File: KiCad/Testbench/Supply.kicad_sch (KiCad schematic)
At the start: 3 parts, among them J21 Conn_02x02_Top_Bottom

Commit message: PCB before first processing
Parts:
- renumbered J21 to J29
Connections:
- net GND is gone; now on net GND-LV_Unfiltered: J29.4 (Pin_4)
- net +24V: now also J29.3 (Pin_3)
- no-connect marks 1 -> 0
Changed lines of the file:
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@@
 	(paper "A4")
+	(junction
+		(at 40.64 44.45)
+		(diameter 0)
+		(color 0 0 0 0)
+	)
 	(junction
 		(at 41.91 66.04)
@@
 	)
 	(junction
+		(at 40.64 46.99)
+		(diameter 0)
+		(color 0 0 0 0)
+	)
+	(junction
 		(at 34.29 55.88)
 		(diameter 0)
 		(color 0 0 0 0)
 	)
-	(no_connect
-		(at 57.15 44.45)
-	)
-	(wire
-		(pts
-			(xy 34.29 46.99) (xy 44.45 46.99)
+	(wire
+		(pts
+			(xy 34.29 46.99) (xy 40.64 46.99)
 		)
 		(stroke
@@
 	(wire
 		(pts
+			(xy 40.64 46.99) (xy 40.64 49.53)
+		)
+		(stroke
+			(width 0)
+			(type default)
+		)
+	)
+	(wire
+		(pts
 			(xy 49.53 59.69) (xy 49.53 66.04)
 		)
@@
 	(wire
 		(pts
-			(xy 74.93 46.99) (xy 74.93 69.85)
+			(xy 62.23 49.53) (xy 62.23 46.99)
 		)
 		(stroke
@@
 	(wire
 		(pts
+			(xy 40.64 46.99) (xy 44.45 46.99)
+		)
+		(stroke
+			(width 0)
+			(type default)
+		)
+	)
+	(wire
+		(pts
 			(xy 34.29 31.75) (xy 34.29 34.29)
 		)
@@
 	(wire
 		(pts
+			(xy 62.23 46.99) (xy 57.15 46.99)
+		)
+		(stroke
+			(width 0)
+			(type default)
+		)
+	)
+	(wire
+		(pts
 			(xy 57.15 66.04) (xy 49.53 66.04)
 		)
@@
 	(wire
 		(pts
+			(xy 40.64 44.45) (xy 40.64 35.56)
+		)
+		(stroke
+			(width 0)
+			(type default)
+		)
+	)
+	(wire
+		(pts
+			(xy 40.64 35.56) (xy 66.04 35.56)
+		)
+		(stroke
+			(width 0)
+			(type default)
+		)
+	)
+	(wire
+		(pts
 			(xy 34.29 46.99) (xy 34.29 55.88)
 		)
@@
 	(wire
 		(pts
+			(xy 40.64 49.53) (xy 62.23 49.53)
+		)
+		(stroke
+			(width 0)
+			(type default)
+		)
+	)
+	(wire
+		(pts
 			(xy 34.29 34.29) (xy 40.64 34.29)
 		)
@@
 	(wire
 		(pts
-			(xy 44.45 44.45) (xy 34.29 44.45)
-		)
-		(stroke
-			(width 0)
-			(type default)
-		)
-	)
-	(wire
-		(pts
-			(xy 57.15 46.99) (xy 74.93 46.99)
+			(xy 40.64 44.45) (xy 34.29 44.45)
+		)
+		(stroke
+			(width 0)
+			(type default)
+		)
+	)
+	(wire
+		(pts
+			(xy 66.04 35.56) (xy 66.04 44.45)
+		)
+		(stroke
+			(width 0)
+			(type default)
+		)
+	)
+	(wire
+		(pts
+			(xy 44.45 44.45) (xy 40.64 44.45)
 		)
 		(stroke
@@
 		(pts
 			(xy 34.29 55.88) (xy 34.29 66.04)
+		)
+		(stroke
+			(width 0)
+			(type default)
+		)
+	)
+	(wire
+		(pts
+			(xy 66.04 44.45) (xy 57.15 44.45)
 		)
 		(stroke
@@
 		)
 	)
-	(label "3-G4"
-		(at 67.31 46.99 0)
-		(fields_autoplaced yes)
-		(effects
-			(font
-				(size 1.27 1.27)
-			)
-			(justify left bottom)
-		)
-	)
 	(label "1-F2"
 		(at 49.53 59.69 0)
@@
 			)
 			(justify left bottom)
-		)
-	)
-	(symbol
-		(lib_id "power:GND")
-		(at 74.93 69.85 0)
-		(unit 1)
-		(exclude_from_sim no)
-		(in_bom yes)
-		(on_board yes)
-		(dnp no)
-		(fields_autoplaced yes)
-		(property "Reference" "#PWR026"
-			(at 74.93 76.2 0)
-			(effects
-				(font
-					(size 1.27 1.27)
-				)
-				(hide yes)
-			)
-		)
-		(property "Value" "GND"
-			(at 74.93 74.93 0)
-			(effects
-				(font
-					(size 1.27 1.27)
-				)
-			)
-		)
-		(property "Footprint" ""
-			(at 74.93 69.85 0)
-			(effects
-				(font
-					(size 1.27 1.27)
-				)
-				(hide yes)
-			)
-		)
-		(property "Datasheet" ""
-			(at 74.93 69.85 0)
-			(effects
-				(font
-					(size 1.27 1.27)
-				)
-				(hide yes)
-			)
-		)
-		(property "Description" "Power symbol creates a global label with name \"GND\" , ground"
-			(at 74.93 69.85 0)
-			(effects
-				(font
-					(size 1.27 1.27)
-				)
-				(hide yes)
-			)
-		)
-		(pin "1"
-		)
-		(instances
-			(project ""
-				(path "/7bff671f-2f7d-4dcb-82cb-7f168fb2ab46/c2512be0-55aa-4b8a-8574-f17326802af0"
-					(reference "#PWR026")
-					(unit 1)
-				)
-			)
 		)
 	)
@@
 		(on_board yes)
 		(dnp no)
-		(property "Reference" "#PWR025"
+		(property "Reference" "#PWR028"
 			(at 49.53 77.47 0)
 			(effects
@@
 			(project "Testbench"
 				(path "/7bff671f-2f7d-4dcb-82cb-7f168fb2ab46/c2512be0-55aa-4b8a-8574-f17326802af0"
-					(reference "#PWR025")
+					(reference "#PWR028")
 					(unit 1)
 				)
@@
 		(dnp no)
 		(fields_autoplaced yes)
-		(property "Reference" "J21"
+		(property "Reference" "J29"
 			(at 50.8 38.1 0)
 			(effects
@@
 			(project ""
 				(path "/7bff671f-2f7d-4dcb-82cb-7f168fb2ab46/c2512be0-55aa-4b8a-8574-f17326802af0"
-					(reference "J21")
+					(reference "J29")
 					(unit 1)
 				)
@@
 		(dnp no)
 		(fields_autoplaced yes)
-		(property "Reference" "#PWR024"
+		(property "Reference" "#PWR027"
 			(at 34.29 35.56 0)
 			(effects
@@
 			(project ""
 				(path "/7bff671f-2f7d-4dcb-82cb-7f168fb2ab46/c2512be0-55aa-4b8a-8574-f17326802af0"
-					(reference "#PWR024")
+					(reference "#PWR027")
 					(unit 1)
 				)

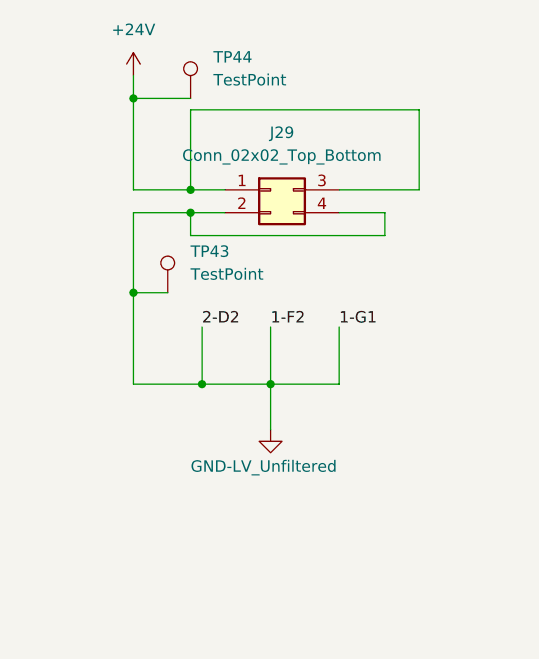
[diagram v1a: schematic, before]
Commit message: Updated for PCBV2 Updated size and added LED.
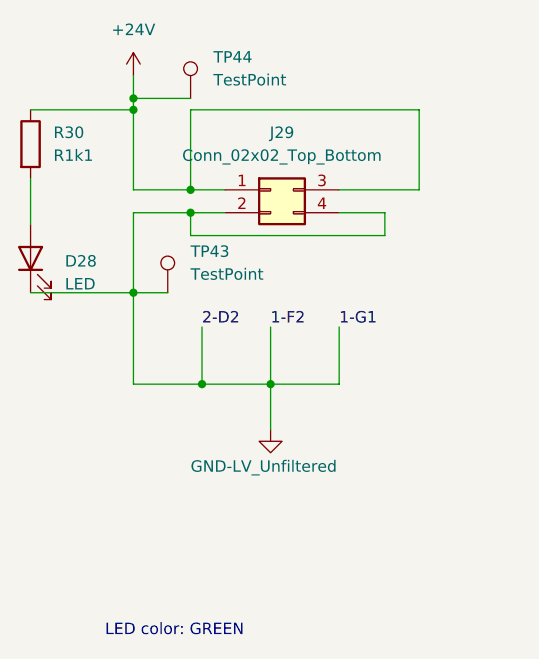
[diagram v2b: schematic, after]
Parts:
- added D28: LED, LED_SMD:LED_0805_2012Metric_Pad1.15x1.40mm_HandSolder, symbol Device:LED
- added R30: R1k1, Resistor_SMD:R_1206_3216Metric_Pad1.30x1.75mm_HandSolder, symbol Device:R
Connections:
- net +24V: now also R30.1
- net GND-LV_Unfiltered: now also D28.1 (K)
- new net: D28.2 (A), R30.2
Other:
- note added: "LED color: GREEN"
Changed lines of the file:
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@@
+	)
+	(junction
+		(at 34.29 35.56)
+		(diameter 0)
+		(color 0 0 0 0)
 	)
 	(junction
@@
 	(wire
 		(pts
+			(xy 22.86 55.88) (xy 34.29 55.88)
+		)
+		(stroke
+			(width 0)
+			(type default)
+		)
+	)
+	(wire
+		(pts
 			(xy 34.29 46.99) (xy 40.64 46.99)
 		)
@@
 	(wire
 		(pts
+			(xy 22.86 43.18) (xy 22.86 48.26)
+		)
+		(stroke
+			(width 0)
+			(type default)
+		)
+	)
+	(wire
+		(pts
 			(xy 62.23 49.53) (xy 62.23 46.99)
 		)
@@
 	(wire
 		(pts
-			(xy 34.29 34.29) (xy 34.29 44.45)
+			(xy 34.29 34.29) (xy 34.29 35.56)
 		)
 		(stroke
@@
 	(wire
 		(pts
+			(xy 22.86 35.56) (xy 34.29 35.56)
+		)
+		(stroke
+			(width 0)
+			(type default)
+		)
+	)
+	(wire
+		(pts
 			(xy 62.23 46.99) (xy 57.15 46.99)
 		)
@@
 	(wire
 		(pts
+			(xy 34.29 35.56) (xy 34.29 44.45)
+		)
+		(stroke
+			(width 0)
+			(type default)
+		)
+	)
+	(wire
+		(pts
 			(xy 57.15 66.04) (xy 49.53 66.04)
 		)
@@
 			(width 0)
 			(type default)
+		)
+	)
+	(text "LED color: GREEN"
+		(exclude_from_sim no)
+		(at 38.862 93.472 0)
+		(effects
+			(font
+				(size 1.27 1.27)
+			)
 		)
 	)
@@
 					(unit 1)
 				)
+			)
+		)
+	)
+	(symbol
+		(lib_id "Device:LED")
+		(at 22.86 52.07 90)
+		(unit 1)
+		(exclude_from_sim no)
+		(in_bom yes)
+		(on_board yes)
+		(dnp no)
+		(fields_autoplaced yes)
+		(property "Reference" "D28"
+			(at 26.67 52.3874 90)
+			(effects
+				(font
+					(size 1.27 1.27)
+				)
+				(justify right)
+			)
+		)
+		(property "Value" "LED"
+			(at 26.67 54.9274 90)
+			(effects
+				(font
+					(size 1.27 1.27)
+				)
+				(justify right)
+			)
+		)
+		(property "Footprint" "LED_SMD:LED_0805_2012Metric_Pad1.15x1.40mm_HandSolder"
+			(at 22.86 52.07 0)
+			(effects
+				(font
+					(size 1.27 1.27)
+				)
+				(hide yes)
+			)
+		)
+		(property "Datasheet" "~"
+			(at 22.86 52.07 0)
+			(effects
+				(font
+					(size 1.27 1.27)
+				)
+				(hide yes)
+			)
+		)
+		(property "Description" "Light emitting diode"
+			(at 22.86 52.07 0)
+			(effects
+				(font
+					(size 1.27 1.27)
+				)
+				(hide yes)
+			)
+		)
+		(pin "2"
+		)
+		(pin "1"
+		)
+		(instances
+			(project "Testbench"
+				(path "/7bff671f-2f7d-4dcb-82cb-7f168fb2ab46/c2512be0-55aa-4b8a-8574-f17326802af0"
+					(reference "D28")
+					(unit 1)
+				)
+			)
+		)
+	)
+	(symbol
+		(lib_id "Device:R")
+		(at 22.86 39.37 0)
+		(unit 1)
+		(exclude_from_sim no)
+		(in_bom yes)
+		(on_board yes)
+		(dnp no)
+		(fields_autoplaced yes)
+		(property "Reference" "R30"
+			(at 25.4 38.0999 0)
+			(effects
+				(font
+					(size 1.27 1.27)
+				)
+				(justify left)
+			)
+		)
+		(property "Value" "R1k1"
+			(at 25.4 40.6399 0)
+			(effects
+				(font
+					(size 1.27 1.27)
+				)
+				(justify left)
+			)
+		)
+		(property "Footprint" "Resistor_SMD:R_1206_3216Metric_Pad1.30x1.75mm_HandSolder"
+			(at 21.082 39.37 90)
+			(effects
+				(font
+					(size 1.27 1.27)
+				)
+				(hide yes)
+			)
+		)
+		(property "Datasheet" "~"
+			(at 22.86 39.37 0)
+			(effects
+				(font
+					(size 1.27 1.27)
+				)
+				(hide yes)
+			)
+		)
+		(property "Description" "Resistor"
+			(at 22.86 39.37 0)
+			(effects
+				(font
+					(size 1.27 1.27)
+				)
+				(hide yes)
+			)
+		)
+		(pin "2"
+		)
+		(pin "1"
+		)
+		(instances
+			(project "Testbench"
+				(path "/7bff671f-2f7d-4dcb-82cb-7f168fb2ab46/c2512be0-55aa-4b8a-8574-f17326802af0"
+					(reference "R30")
+					(unit 1)
+				)
